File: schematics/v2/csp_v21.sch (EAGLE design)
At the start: 65 parts, among them IC1 74AHC1G08DCK, IC2 74HCT04D, IC3 PCA9555PW, IC4 LM339D, J1 2X20-CHIP2X20-SMT-CHIP, Q1 BSS84, Q2 BSS123, U2 DS2431P

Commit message: added v2.1, with 5V switchable to avoid discharge
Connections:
- net VCC3V3: now also C2.1, C4.1, L2.2
- net VCC5V: no longer C2.1, C4.1, L2.2
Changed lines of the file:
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@@
 <part name="U$5" library="JKW_CHIP" deviceset="LOGO_10X10_SILK" device=""/>
 <part name="SUPPLY10" library="Keyboard v0.3" deviceset="VCC3V3" device=""/>
-<part name="SUPPLY11" library="Keyboard v0.3" deviceset="VCC5V" device=""/>
 <part name="U$6" library="Keyboard v0.2" deviceset="GND" device=""/>
 <part name="SUPPLY12" library="Keyboard v0.3" deviceset="VCC3V3" device=""/>
@@
 <instance part="U$5" gate="G$1" x="523.24" y="66.04"/>
 <instance part="SUPPLY10" gate="+5V" x="327.66" y="137.16"/>
-<instance part="SUPPLY11" gate="+5V" x="406.4" y="264.16"/>
 <instance part="U$6" gate="M" x="586.74" y="106.68"/>
 <instance part="SUPPLY12" gate="+5V" x="414.02" y="287.02"/>
@@
 <pinref part="U$27" gate="G$1" pin="IN"/>
 <pinref part="SUPPLY12" gate="+5V" pin="VCC3V3"/>
-<wire x1="422.91" y1="281.94" x2="414.02" y2="281.94" width="0.1524" layer="91"/>
+<wire x1="422.91" y1="281.94" x2="419.1" y2="281.94" width="0.1524" layer="91"/>
+<wire x1="419.1" y1="281.94" x2="414.02" y2="281.94" width="0.1524" layer="91"/>
 <wire x1="414.02" y1="281.94" x2="414.02" y2="284.48" width="0.1524" layer="91"/>
+<pinref part="C2" gate="G$1" pin="1"/>
+<pinref part="C4" gate="G$1" pin="1"/>
+<wire x1="419.1" y1="254" x2="419.1" y2="261.62" width="0.1524" layer="91"/>
+<wire x1="419.1" y1="261.62" x2="429.26" y2="261.62" width="0.1524" layer="91"/>
+<wire x1="429.26" y1="261.62" x2="429.26" y2="254" width="0.1524" layer="91"/>
+<junction x="429.26" y="261.62"/>
+<wire x1="429.26" y1="261.62" x2="435.61" y2="261.62" width="0.1524" layer="91"/>
+<pinref part="L2" gate="G$1" pin="2"/>
+<label x="408.94" y="262.89" size="1.778" layer="95"/>
+<wire x1="419.1" y1="261.62" x2="419.1" y2="281.94" width="0.1524" layer="91"/>
+<junction x="419.1" y="261.62"/>
+<junction x="419.1" y="281.94"/>
 </segment>
 <segment>
@@
 </segment>
 <segment>
-<pinref part="SUPPLY11" gate="+5V" pin="VCC5V"/>
-<wire x1="406.4" y1="261.62" x2="419.1" y2="261.62" width="0.1524" layer="91"/>
-<pinref part="C2" gate="G$1" pin="1"/>
-<pinref part="C4" gate="G$1" pin="1"/>
-<wire x1="419.1" y1="254" x2="419.1" y2="261.62" width="0.1524" layer="91"/>
-<junction x="419.1" y="261.62"/>
-<wire x1="419.1" y1="261.62" x2="429.26" y2="261.62" width="0.1524" layer="91"/>
-<wire x1="429.26" y1="261.62" x2="429.26" y2="254" width="0.1524" layer="91"/>
-<junction x="429.26" y="261.62"/>
-<wire x1="429.26" y1="261.62" x2="435.61" y2="261.62" width="0.1524" layer="91"/>
-<pinref part="L2" gate="G$1" pin="2"/>
-<label x="408.94" y="262.89" size="1.778" layer="95"/>
-</segment>
-<segment>

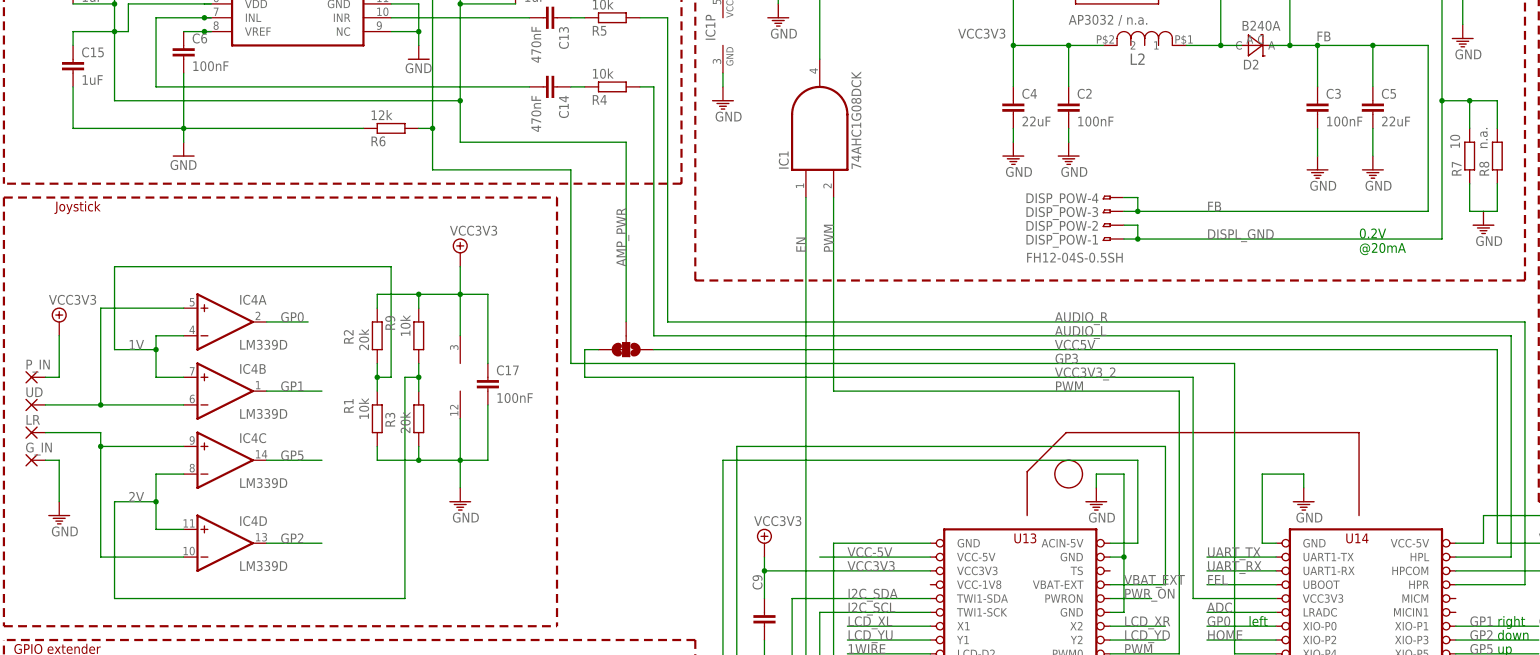
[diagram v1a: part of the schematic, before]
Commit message: Fixed Op-amp, position of thumb still wrong
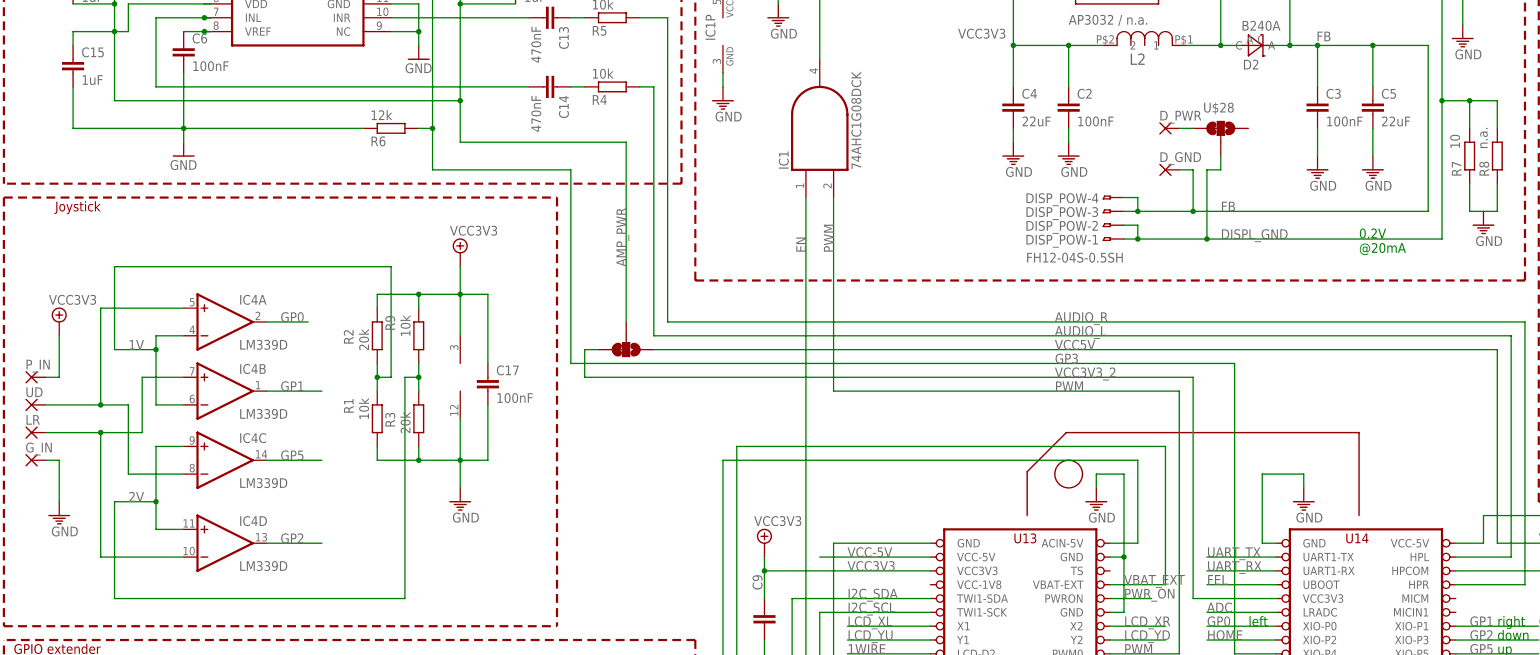
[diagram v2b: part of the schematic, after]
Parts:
- added D_GND: D_GND, JKW_CHIP:SMD1.36X3
- added D_PWR: D_PWR, JKW_CHIP:SMD1.36X3
- added U$28: SMD_SJ_3WAY_CLOSED, JKW_CHIP:SMD_SJ_3WAY_CLOSED
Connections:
- new net N$28: D_PWR.P, U$28.1
- net 1V: now also IC4B.-IN; no longer IC4B.+IN
- net 2V: now also IC4C.+IN; no longer IC4C.-IN
- net DISPL_GND: now also U$28.2
- net FB: now also D_GND.P
- net N$30: now also IC4C.-IN; no longer IC4B.-IN
- net N$31: now also IC4B.+IN; no longer IC4C.+IN
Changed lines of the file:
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@@
 <?xml version="1.0" encoding="utf-8"?>
 <!DOCTYPE eagle SYSTEM "eagle.dtd">
-<eagle version="7.7.0">
+<eagle version="7.6.0">
 <drawing>
 <settings>
@@
 <part name="U$26" library="Keyboard v0.2" deviceset="GND" device=""/>
 <part name="R11" library="rcl" deviceset="R-EU_" device="R0805" value="12k"/>
+<part name="D_PWR" library="JKW_CHIP" deviceset="SMD1.36X3" device="" value="D_PWR"/>
+<part name="D_GND" library="JKW_CHIP" deviceset="SMD1.36X3" device="" value="D_GND"/>
+<part name="U$28" library="JKW_CHIP" deviceset="SMD_SJ_3WAY_CLOSED" device=""/>
 </parts>
 <sheets>
@@
 <attribute name="VALUE" x="547.37" y="170.942" size="1.778" layer="96" rot="MR180"/>
 </instance>
+<instance part="D_PWR" gate="1" x="447.04" y="246.38" smashed="yes" rot="MR180">
+<attribute name="NAME" x="445.897" y="249.6058" size="1.778" layer="95" rot="MR180"/>
+</instance>
+<instance part="D_GND" gate="1" x="447.04" y="238.76" smashed="yes" rot="MR180">
+<attribute name="NAME" x="445.897" y="241.9858" size="1.778" layer="95" rot="MR180"/>
+</instance>
+<instance part="U$28" gate="G$1" x="457.2" y="246.38" smashed="yes" rot="R90">
+<attribute name="NAME" x="459.74" y="251.079" size="1.778" layer="95" rot="R180"/>
+</instance>
 </instances>
 <busses>
@@
 <wire x1="439.42" y1="226.06" x2="441.96" y2="226.06" width="0.1524" layer="91"/>
 <pinref part="U$27" gate="G$1" pin="FB"/>
-<wire x1="441.96" y1="226.06" x2="497.84" y2="226.06" width="0.1524" layer="91"/>
+<wire x1="441.96" y1="226.06" x2="454.66" y2="226.06" width="0.1524" layer="91"/>
+<wire x1="454.66" y1="226.06" x2="497.84" y2="226.06" width="0.1524" layer="91"/>
 <wire x1="497.84" y1="226.06" x2="497.84" y2="251.46" width="0.1524" layer="91"/>
 <wire x1="497.84" y1="251.46" x2="502.92" y2="251.46" width="0.1524" layer="91"/>
@@
 <wire x1="502.92" y1="251.46" x2="502.92" y2="246.38" width="0.1524" layer="91"/>
 <junction x="502.92" y="251.46"/>
-<label x="454.66" y="226.06" size="1.778" layer="95"/>
+<label x="457.2" y="226.06" size="1.778" layer="95"/>
 <pinref part="R8" gate="G$1" pin="2"/>
 <wire x1="508" y1="246.38" x2="508" y2="251.46" width="0.1524" layer="91"/>
@@
 <junction x="441.96" y="226.06"/>
 <junction x="497.84" y="251.46"/>
+<wire x1="454.66" y1="226.06" x2="454.66" y2="238.76" width="0.1524" layer="91"/>
+<pinref part="U$28" gate="G$1" pin="2"/>
+<wire x1="454.66" y1="238.76" x2="457.2" y2="238.76" width="0.1524" layer="91"/>
+<wire x1="457.2" y1="238.76" x2="457.2" y2="241.3" width="0.1524" layer="91"/>
+<junction x="454.66" y="226.06"/>
 </segment>
 </net>
@@
 <junction x="485.14" y="261.62"/>
 <pinref part="D2" gate="G$1" pin="C"/>
-<wire x1="441.96" y1="231.14" x2="495.3" y2="231.14" width="0.1524" layer="91"/>
+<wire x1="441.96" y1="231.14" x2="452.12" y2="231.14" width="0.1524" layer="91"/>
 <pinref part="U$27" gate="G$1" pin="OV"/>
+<wire x1="452.12" y1="231.14" x2="495.3" y2="231.14" width="0.1524" layer="91"/>
 <wire x1="453.39" y1="281.94" x2="469.9" y2="281.94" width="0.1524" layer="91"/>
 <pinref part="C8" gate="G$1" pin="1"/>
@@
 <wire x1="439.42" y1="231.14" x2="441.96" y2="231.14" width="0.1524" layer="91"/>
 <junction x="441.96" y="231.14"/>
-<label x="454.66" y="231.14" size="1.778" layer="95"/>
+<label x="457.2" y="231.14" size="1.778" layer="95"/>
+<pinref part="D_GND" gate="1" pin="P"/>
+<wire x1="449.58" y1="238.76" x2="452.12" y2="238.76" width="0.1524" layer="91"/>
+<wire x1="452.12" y1="238.76" x2="452.12" y2="231.14" width="0.1524" layer="91"/>
+<junction x="452.12" y="231.14"/>
 </segment>
 </net>
@@
 <pinref part="IC4" gate="A" pin="-IN"/>
 <wire x1="261.62" y1="208.28" x2="266.7" y2="208.28" width="0.1524" layer="91"/>
-<pinref part="IC4" gate="B" pin="+IN"/>
-<wire x1="266.7" y1="200.66" x2="261.62" y2="200.66" width="0.1524" layer="91"/>
-<wire x1="261.62" y1="200.66" x2="261.62" y2="205.74" width="0.1524" layer="91"/>
 <junction x="261.62" y="205.74"/>
 <label x="256.54" y="205.74" size="1.778" layer="95"/>
@@
 <wire x1="254" y1="220.98" x2="254" y2="205.74" width="0.1524" layer="91"/>
 <junction x="302.26" y="200.66"/>
+<pinref part="IC4" gate="B" pin="-IN"/>
+<wire x1="266.7" y1="195.58" x2="261.62" y2="195.58" width="0.1524" layer="91"/>
+<wire x1="261.62" y1="195.58" x2="261.62" y2="205.74" width="0.1524" layer="91"/>
 </segment>
 </net>
@@
 <wire x1="261.62" y1="172.72" x2="266.7" y2="172.72" width="0.1524" layer="91"/>
 <wire x1="261.62" y1="172.72" x2="261.62" y2="177.8" width="0.1524" layer="91"/>
-<pinref part="IC4" gate="C" pin="-IN"/>
-<wire x1="261.62" y1="177.8" x2="261.62" y2="182.88" width="0.1524" layer="91"/>
-<wire x1="261.62" y1="182.88" x2="266.7" y2="182.88" width="0.1524" layer="91"/>
 <label x="256.54" y="177.8" size="1.778" layer="95"/>
 <pinref part="R9" gate="G$1" pin="2"/>
@@
 <wire x1="254" y1="177.8" x2="261.62" y2="177.8" width="0.1524" layer="91"/>
 <junction x="261.62" y="177.8"/>
+<pinref part="IC4" gate="C" pin="+IN"/>
+<wire x1="266.7" y1="187.96" x2="261.62" y2="187.96" width="0.1524" layer="91"/>
+<wire x1="261.62" y1="187.96" x2="261.62" y2="177.8" width="0.1524" layer="91"/>
 </segment>
 </net>
@@
 <pinref part="IC4" gate="A" pin="+IN"/>
 <wire x1="251.46" y1="213.36" x2="266.7" y2="213.36" width="0.1524" layer="91"/>
-<pinref part="IC4" gate="B" pin="-IN"/>
-<wire x1="266.7" y1="195.58" x2="251.46" y2="195.58" width="0.1524" layer="91"/>
+<wire x1="251.46" y1="195.58" x2="256.54" y2="195.58" width="0.1524" layer="91"/>
+<wire x1="256.54" y1="195.58" x2="256.54" y2="182.88" width="0.1524" layer="91"/>
 <junction x="251.46" y="195.58"/>
+<pinref part="IC4" gate="C" pin="-IN"/>
+<wire x1="266.7" y1="182.88" x2="256.54" y2="182.88" width="0.1524" layer="91"/>
 </segment>
 </net>
@@
 <pinref part="LR" gate="1" pin="P"/>
 <wire x1="241.3" y1="190.5" x2="251.46" y2="190.5" width="0.1524" layer="91"/>
-<wire x1="251.46" y1="190.5" x2="251.46" y2="187.96" width="0.1524" layer="91"/>
-<pinref part="IC4" gate="C" pin="+IN"/>
-<wire x1="251.46" y1="187.96" x2="266.7" y2="187.96" width="0.1524" layer="91"/>
 <pinref part="IC4" gate="D" pin="-IN"/>
 <wire x1="266.7" y1="167.64" x2="251.46" y2="167.64" width="0.1524" layer="91"/>
-<wire x1="251.46" y1="167.64" x2="251.46" y2="187.96" width="0.1524" layer="91"/>
-<junction x="251.46" y="187.96"/>
+<wire x1="251.46" y1="167.64" x2="251.46" y2="190.5" width="0.1524" layer="91"/>
+<wire x1="251.46" y1="190.5" x2="259.08" y2="190.5" width="0.1524" layer="91"/>
+<junction x="251.46" y="190.5"/>
+<pinref part="IC4" gate="B" pin="+IN"/>
+<wire x1="266.7" y1="200.66" x2="259.08" y2="200.66" width="0.1524" layer="91"/>
+<wire x1="259.08" y1="200.66" x2="259.08" y2="190.5" width="0.1524" layer="91"/>
 </segment>
 </net>
@@
 </segment>
 </net>
+<net name="N$28" class="0">
+<segment>
+<pinref part="D_PWR" gate="1" pin="P"/>
+<pinref part="U$28" gate="G$1" pin="1"/>
+<wire x1="452.12" y1="246.38" x2="449.58" y2="246.38" width="0.1524" layer="91"/>
+</segment>
+</net>
